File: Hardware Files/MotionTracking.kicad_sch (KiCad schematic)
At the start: 18 parts, among them J1 Micro_SD_Card_Det1, J2 USB_B_Micro, U1 LSM6DSV16XTR, U4 STM32F411RET6, Y1 16MHz

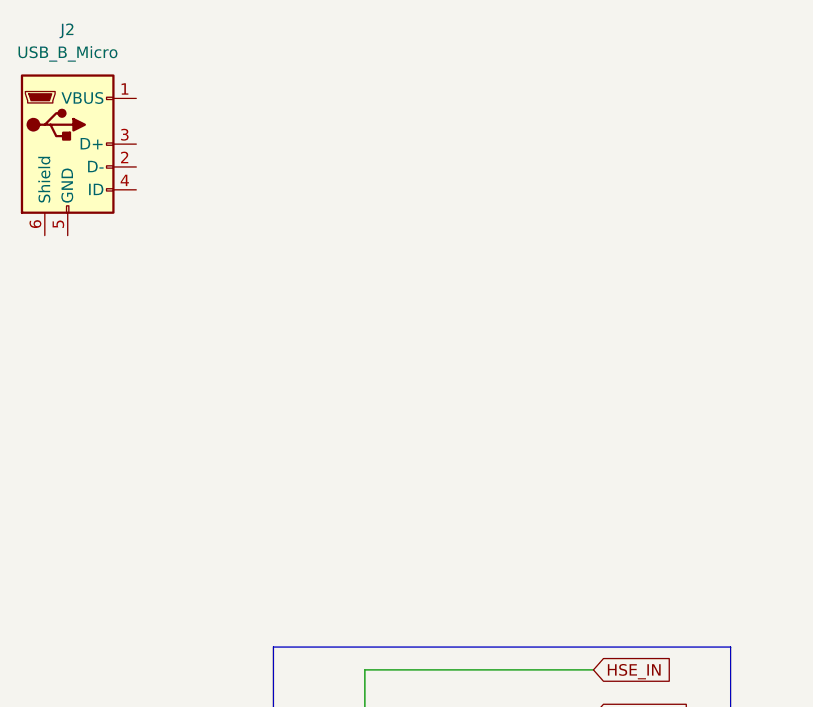
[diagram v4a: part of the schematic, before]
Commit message: Update MotionTracking.kicad_sch
Added buck converter components.
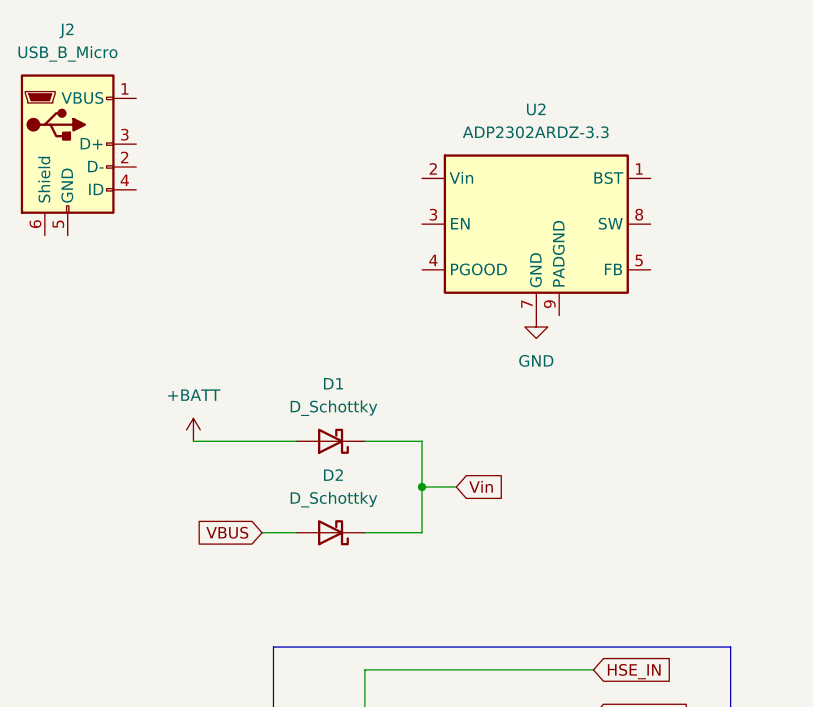
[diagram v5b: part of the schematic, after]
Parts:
- added D1, D2: D_Schottky, symbol Device:D_Schottky
- added U2: ADP2302ARDZ-3.3, Package_SO:SOIC-8-1EP_3.9x4.9mm_P1.27mm_EP2.29x3mm, symbol Regulator_Switching:ADP2302ARDZ-3.3
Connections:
- net GND: now also U2.7 (GND)
- new net +BATT: D1.2 (A)
- new net VBUS: D2.2 (A)
- new net Vin: D1.1 (K), D2.1 (K)
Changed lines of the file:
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@@
   (junction (at 182.88 43.18) (diameter 0) (color 0 0 0 0)
+  )
+  (junction (at 64.77 66.04) (diameter 0) (color 0 0 0 0)
   )
   (junction (at 134.62 71.12) (diameter 0) (color 0 0 0 0)
@@
   (no_connect (at 200.66 144.78))
   (no_connect (at 266.7 144.78))
+  (wire (pts (xy 46.99 71.12) (xy 50.8 71.12))
+    (stroke (width 0) (type default))
+  )
   (wire (pts (xy 137.16 71.12) (xy 137.16 73.66))
     (stroke (width 0) (type default))
@@
     (stroke (width 0) (type default))
   )
+  (wire (pts (xy 39.37 60.96) (xy 50.8 60.96))
+    (stroke (width 0) (type default))
+  )
   (wire (pts (xy 259.08 40.64) (xy 259.08 35.56))
     (stroke (width 0) (type default))
@@
     (stroke (width 0) (type default))
   )
+  (wire (pts (xy 64.77 66.04) (xy 68.58 66.04))
+    (stroke (width 0) (type default))
+  )
   (wire (pts (xy 137.16 167.64) (xy 137.16 172.72))
     (stroke (width 0) (type default))
@@
     (stroke (width 0) (type default))
   )
+  (wire (pts (xy 64.77 66.04) (xy 64.77 71.12))
+    (stroke (width 0) (type default))
+  )
   (wire (pts (xy 78.74 99.06) (xy 78.74 101.6))
     (stroke (width 0) (type default))
   )
+  (wire (pts (xy 58.42 71.12) (xy 64.77 71.12))
+    (stroke (width 0) (type default))
+  )
   (wire (pts (xy 246.38 43.18) (xy 246.38 40.64))
     (stroke (width 0) (type default))
@@
     (stroke (width 0) (type default))
   )
+  (wire (pts (xy 64.77 60.96) (xy 58.42 60.96))
+    (stroke (width 0) (type default))
+  )
   (wire (pts (xy 170.18 33.02) (xy 182.88 33.02))
     (stroke (width 0) (type default))
@@
   )
   (wire (pts (xy 83.82 91.44) (xy 78.74 91.44))
+    (stroke (width 0) (type default))
+  )
+  (wire (pts (xy 64.77 60.96) (xy 64.77 66.04))
     (stroke (width 0) (type default))
   )
@@
     )
   )
+  (global_label "VBUS" (shape input) (at 46.99 71.12 180) (fields_autoplaced)
+    (effects (font (size 1.27 1.27)) (justify right))
+    (property "Intersheetrefs" "${INTERSHEET_REFS}" (at 39.1062 71.12 0)
+      (effects (font (size 1.27 1.27)) (justify right) hide)
+    )
+  )
   (global_label "HSE_OUT" (shape input) (at 83.82 91.44 0) (fields_autoplaced)
     (effects (font (size 1.27 1.27)) (justify left))
@@
     )
   )
+  (global_label "Vin" (shape input) (at 68.58 66.04 0) (fields_autoplaced)
+    (effects (font (size 1.27 1.27)) (justify left))
+    (property "Intersheetrefs" "${INTERSHEET_REFS}" (at 74.4076 66.04 0)
+      (effects (font (size 1.27 1.27)) (justify left) hide)
+    )
+  )
   (global_label "SWDIO" (shape input) (at 154.94 111.76 0) (fields_autoplaced)
     (effects (font (size 1.27 1.27)) (justify left))
@@
     (property "Intersheetrefs" "${INTERSHEET_REFS}" (at 167.7828 96.52 0)
       (effects (font (size 1.27 1.27)) (justify left) hide)
+    )
+  )
+  (symbol (lib_id "power:+BATT") (at 39.37 60.96 0) (unit 1)
+    (in_bom yes) (on_board yes) (dnp no) (fields_autoplaced)
+    (property "Reference" "#PWR018" (at 39.37 64.77 0)
+      (effects (font (size 1.27 1.27)) hide)
+    )
+    (property "Value" "+BATT" (at 39.37 55.88 0)
+      (effects (font (size 1.27 1.27)))
+    )
+    (property "Footprint" "" (at 39.37 60.96 0)
+      (effects (font (size 1.27 1.27)) hide)
+    )
+    (property "Datasheet" "" (at 39.37 60.96 0)
+      (effects (font (size 1.27 1.27)) hide)
+    )
+    (pin "1")
+    (instances
+      (project "MotionTracking"
+        (path "/111120b9-36de-4e64-8ed5-7419f276010e"
+          (reference "#PWR018") (unit 1)
+        )
+      )
     )
   )
@@
         (path "/111120b9-36de-4e64-8ed5-7419f276010e"
           (reference "C8") (unit 1)
+        )
+      )
+    )
+  )
+  (symbol (lib_id "Device:D_Schottky") (at 54.61 60.96 180) (unit 1)
+    (in_bom yes) (on_board yes) (dnp no) (fields_autoplaced)
+    (property "Reference" "D1" (at 54.9275 54.61 0)
+      (effects (font (size 1.27 1.27)))
+    )
+    (property "Value" "D_Schottky" (at 54.9275 57.15 0)
+      (effects (font (size 1.27 1.27)))
+    )
+    (property "Footprint" "" (at 54.61 60.96 0)
+      (effects (font (size 1.27 1.27)) hide)
+    )
+    (property "Datasheet" "~" (at 54.61 60.96 0)
+      (effects (font (size 1.27 1.27)) hide)
+    )
+    (pin "2")
+    (pin "1")
+    (instances
+      (project "MotionTracking"
+        (path "/111120b9-36de-4e64-8ed5-7419f276010e"
+          (reference "D1") (unit 1)
         )
       )
@@
     )
   )
+  (symbol (lib_id "power:GND") (at 77.47 46.99 0) (unit 1)
+    (in_bom yes) (on_board yes) (dnp no) (fields_autoplaced)
+    (property "Reference" "#PWR017" (at 77.47 53.34 0)
+      (effects (font (size 1.27 1.27)) hide)
+    )
+    (property "Value" "GND" (at 77.47 52.07 0)
+      (effects (font (size 1.27 1.27)))
+    )
+    (property "Footprint" "" (at 77.47 46.99 0)
+      (effects (font (size 1.27 1.27)) hide)
+    )
+    (property "Datasheet" "" (at 77.47 46.99 0)
+      (effects (font (size 1.27 1.27)) hide)
+    )
+    (pin "1")
+    (instances
+      (project "MotionTracking"
+        (path "/111120b9-36de-4e64-8ed5-7419f276010e"
+          (reference "#PWR017") (unit 1)
+        )
+      )
+    )
+  )
   (symbol (lib_id "Connector:Micro_SD_Card_Det1") (at 231.14 91.44 180) (unit 1)
     (in_bom yes) (on_board yes) (dnp no) (fields_autoplaced)
@@
     )
   )
+  (symbol (lib_id "Device:D_Schottky") (at 54.61 71.12 180) (unit 1)
+    (in_bom yes) (on_board yes) (dnp no) (fields_autoplaced)
+    (property "Reference" "D2" (at 54.9275 64.77 0)
+      (effects (font (size 1.27 1.27)))
+    )
+    (property "Value" "D_Schottky" (at 54.9275 67.31 0)
+      (effects (font (size 1.27 1.27)))
+    )
+    (property "Footprint" "" (at 54.61 71.12 0)
+      (effects (font (size 1.27 1.27)) hide)
+    )
+    (property "Datasheet" "~" (at 54.61 71.12 0)
+      (effects (font (size 1.27 1.27)) hide)
+    )
+    (pin "2")
+    (pin "1")
+    (instances
+      (project "MotionTracking"
+        (path "/111120b9-36de-4e64-8ed5-7419f276010e"
+          (reference "D2") (unit 1)
+        )
+      )
+    )
+  )
   (symbol (lib_id "Device:C_Small") (at 147.32 38.1 0) (unit 1)
     (in_bom yes) (on_board yes) (dnp no) (fields_autoplaced)
@@
         )
       )
+    )
+  )
+  (symbol (lib_id "Regulator_Switching:ADP2302ARDZ-3.3") (at 77.47 36.83 0) (unit 1)
+    (in_bom yes) (on_board yes) (dnp no) (fields_autoplaced)
+    (property "Reference" "U2" (at 77.47 24.13 0)
+      (effects (font (size 1.27 1.27)))
+    )
+    (property "Value" "ADP2302ARDZ-3.3" (at 77.47 26.67 0)
+      (effects (font (size 1.27 1.27)))
+    )
+    (property "Footprint" "Package_SO:SOIC-8-1EP_3.9x4.9mm_P1.27mm_EP2.29x3mm" (at 81.28 45.72 0)
+      (effects (font (size 1.27 1.27)) (justify left) hide)
+    )
+    (property "Datasheet" "https://www.analog.com/media/en/technical-documentation/data-sheets/ADP2302_2303.pdf" (at 72.39 21.59 0)
+      (effects (font (size 1.27 1.27)) hide)
+    )
+    (pin "1")
+    (pin "7")
+    (pin "9")
+    (pin "8")
+    (pin "3")
+    (pin "6")
+    (pin "5")
+    (pin "2")
+    (pin "4")
+    (instances
+      (project "MotionTracking"
+        (path "/111120b9-36de-4e64-8ed5-7419f276010e"
+          (reference "U2") (unit 1)
+        )
+      )

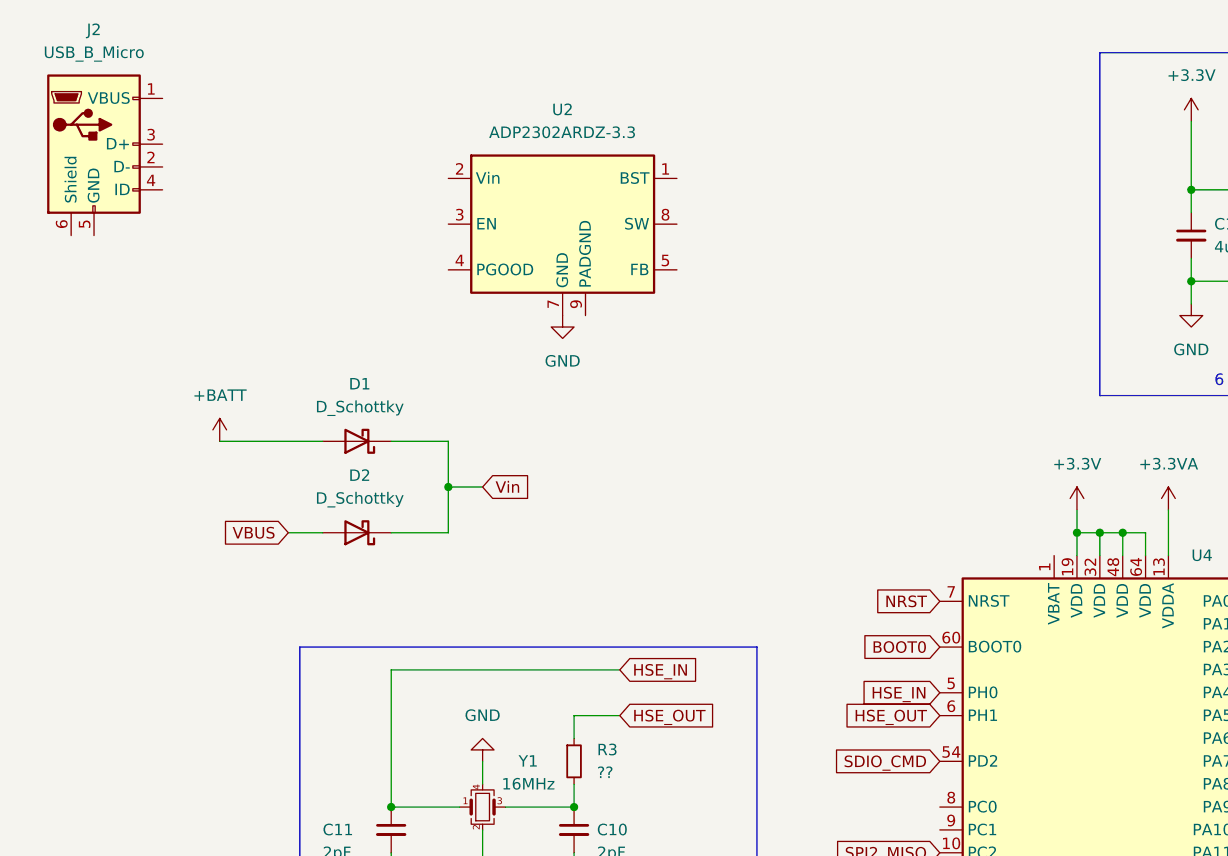
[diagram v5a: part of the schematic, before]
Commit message: Updated MicroUSB and Buck Coverter
- Added NCF flag to shield pin on microUSB

- Added 10uF capacitor to Vin on buck converter to absorb ripple current
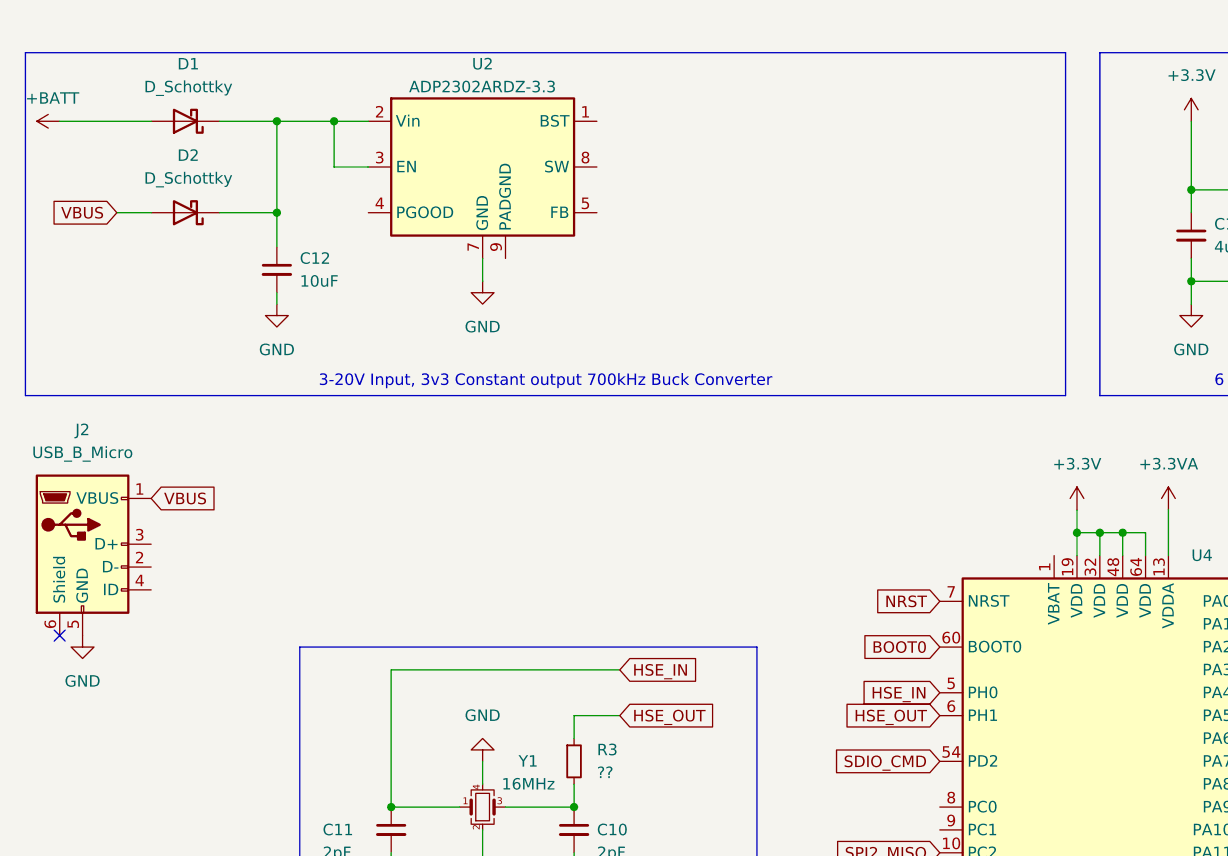
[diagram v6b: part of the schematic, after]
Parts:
- added C12: 10uF, symbol Device:C_Small
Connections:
- net Vin is gone; now on an unnamed net: D1.1 (K), D2.1 (K)
- net GND: now also J2.5 (GND), C12.2
- net VBUS: now also J2.1 (VBUS)
- net at U2.2 (Vin): now also U2.3 (EN), C12.1
- no-connect marks 7 -> 8
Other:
- moved on the sheet: D1, D2, J2, U2

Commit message: Other buck converter changes? or just an autosave?
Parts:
- removed C12: 10uF, symbol Device:C_Small
- added C12: 0.1uF, symbol Device:C
- added D3, D4: D_Schottky, symbol Device:D_Schottky
- added L2: ~1.85uH, symbol Device:L
- added R1: 3.17M, symbol Device:R
- added Rbot1: 10.2k, symbol Device:R
- added Rtop1: 31.6k, symbol Device:R
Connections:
- net GND: now also D4.2 (A), Rbot1.2
- net at D1.1 (K), D2.1 (K), U2.2 (Vin): now also D3.2 (A), R1.2; no longer U2.3 (EN)
- net at U2.1 (BST): now also C12.1, D3.1 (K)
- net at U2.5 (FB): now also Rbot1.1, Rtop1.1
- net at U2.8 (SW): now also C12.2, D4.1 (K), L2.1
- new net: R1.1, U2.3 (EN)
- new net Vout: L2.2, Rtop1.2
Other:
- moved on the sheet: J2
